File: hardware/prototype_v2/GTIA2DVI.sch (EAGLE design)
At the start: 25 parts, among them IC2 74AC541DW, IC4 GTIA, IC5 GTIA

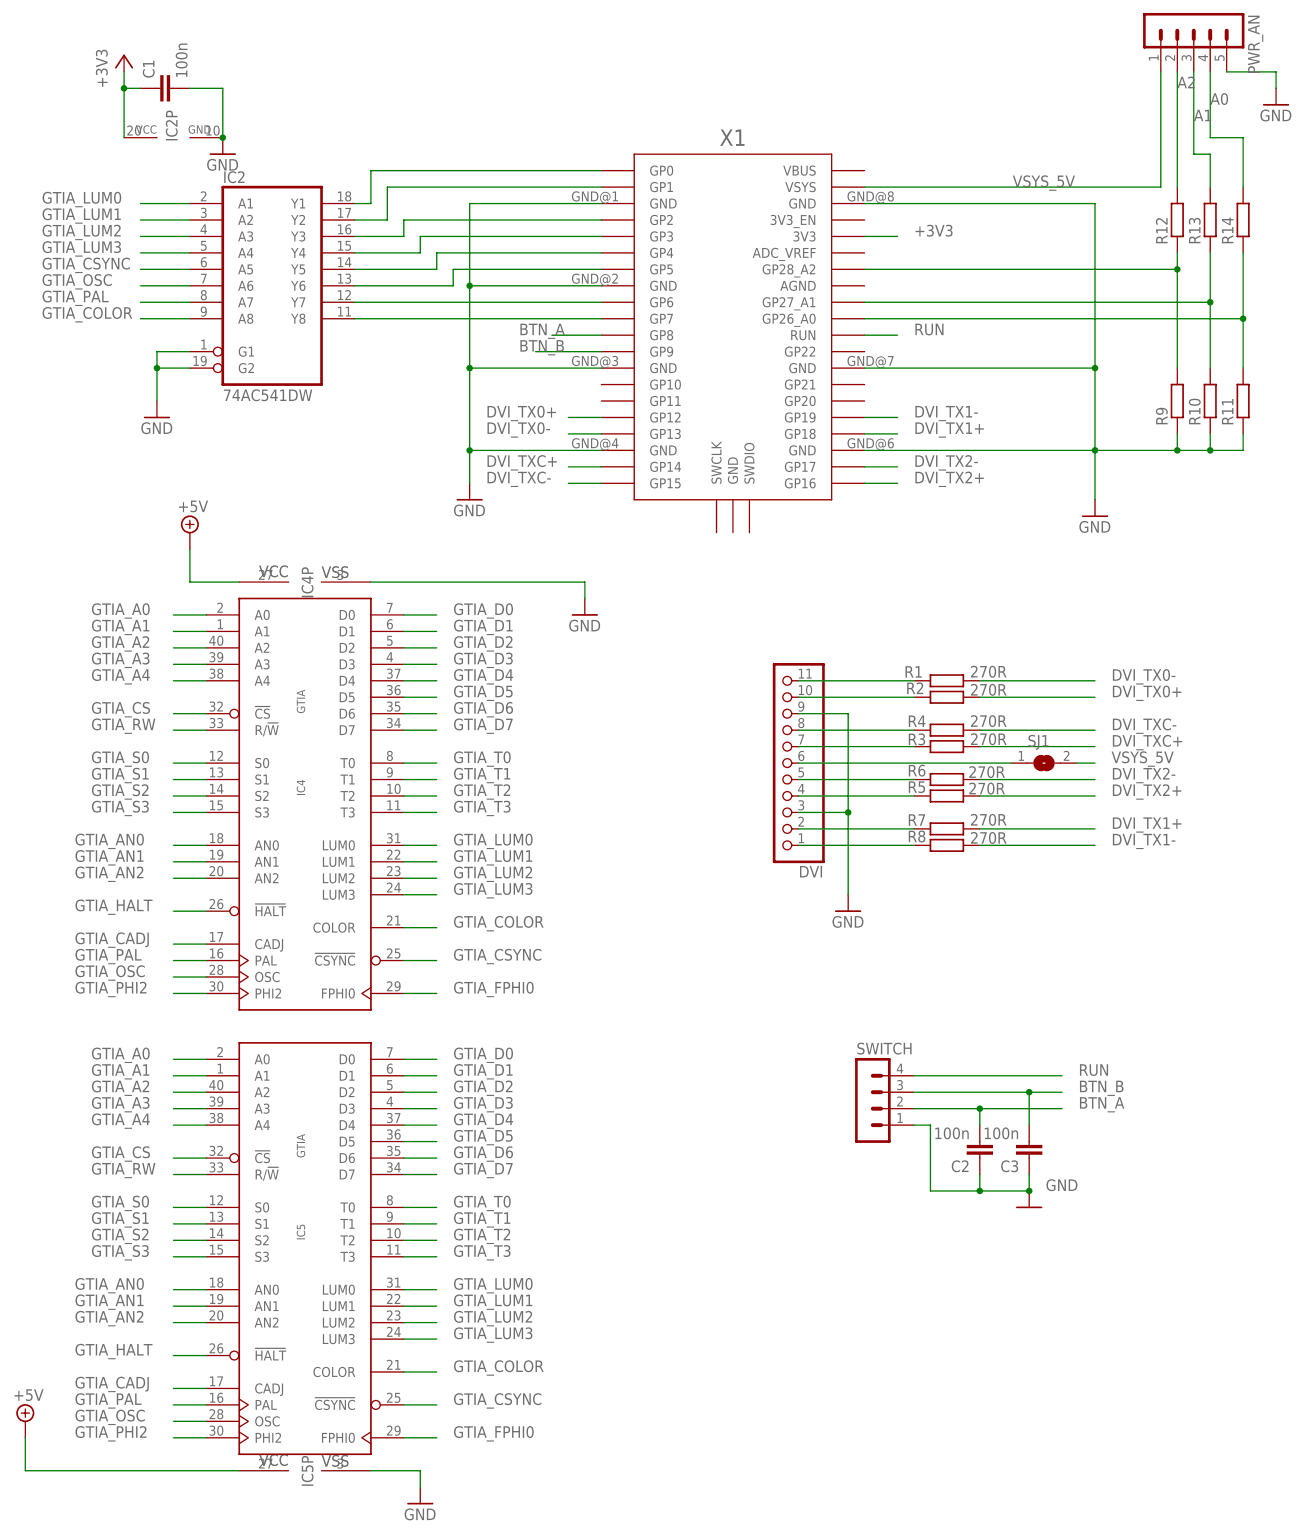
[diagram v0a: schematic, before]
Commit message: moved to hardware UART buttons and UART pins changed
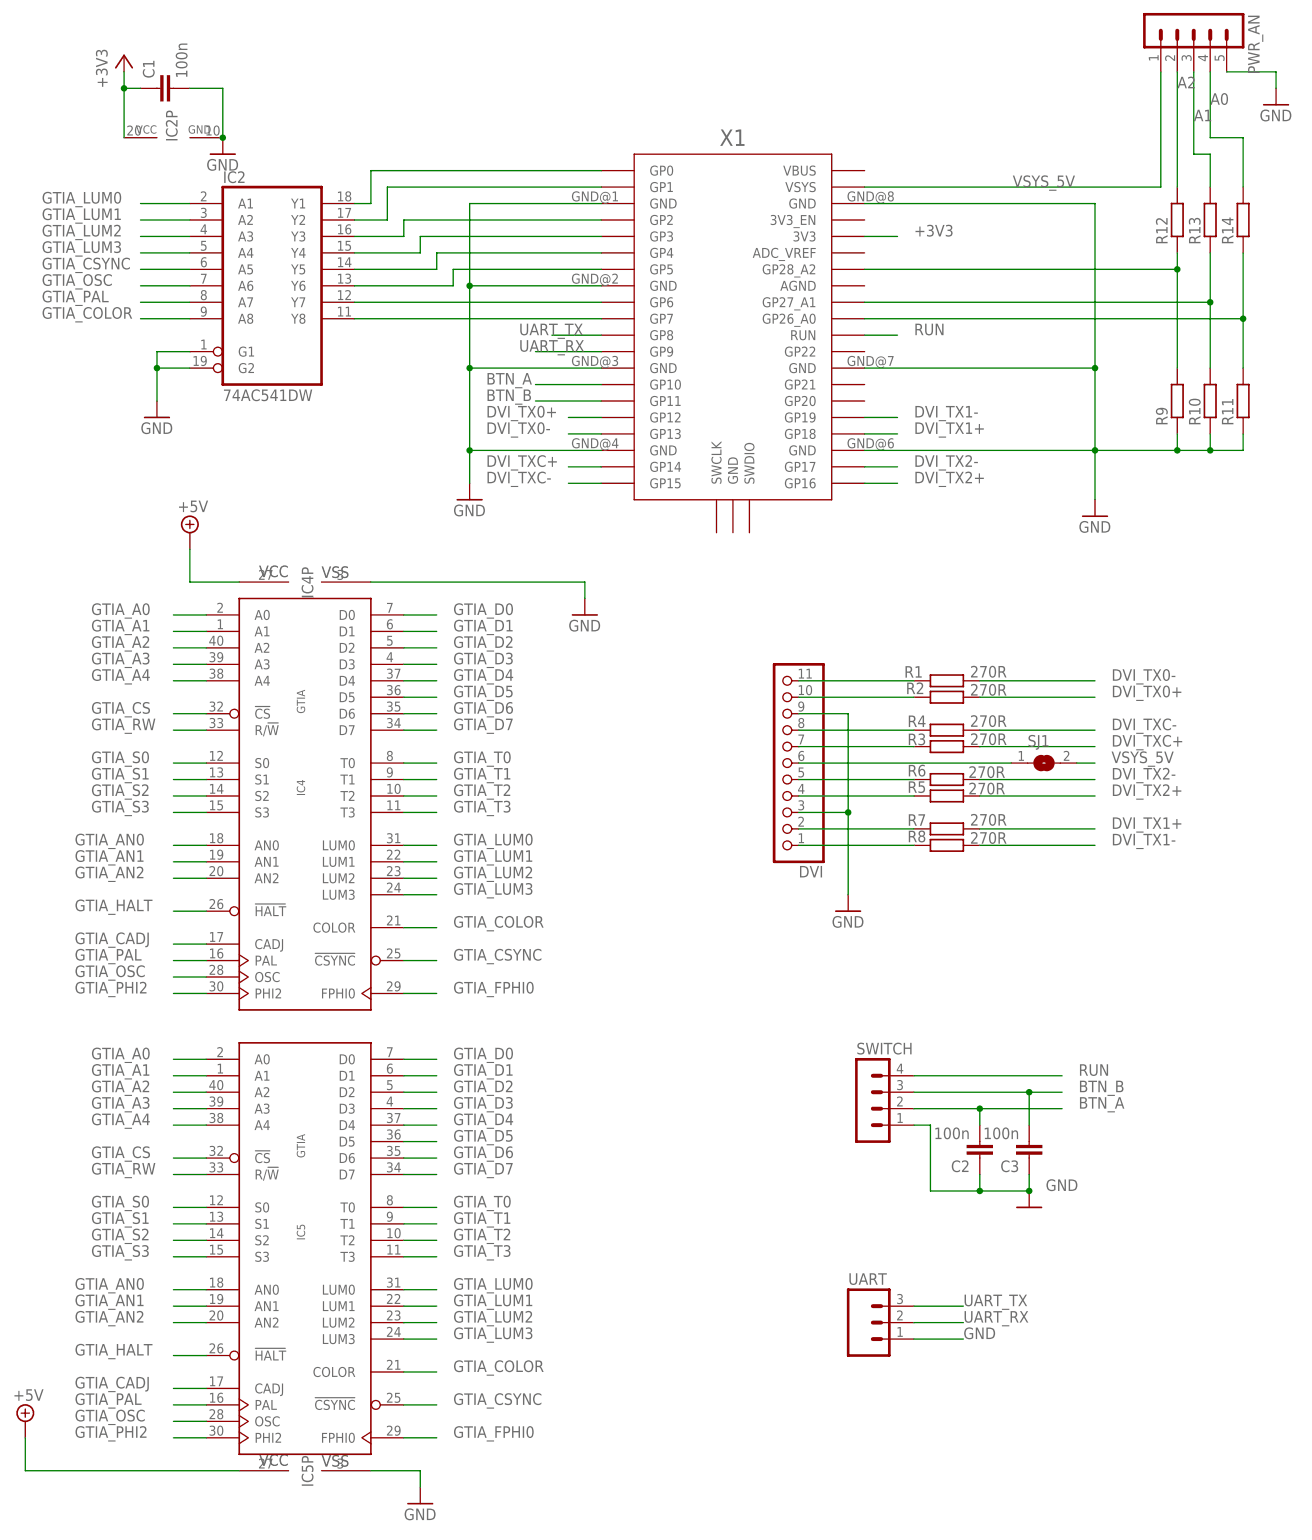
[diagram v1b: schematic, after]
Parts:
- added UART: (no value), con-amp-quick:MA03
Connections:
- new net UART_RX: UART.2, X1.GP9
- new net UART_TX: UART.3, X1.GP8
- net BTN_A: now also X1.GP10; no longer X1.GP8
- net BTN_B: now also X1.GP11; no longer X1.GP9
- net GND: now also UART.1
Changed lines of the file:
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@@
 <part name="C3" library="rcl" library_urn="urn:adsk.eagle:library:334" deviceset="C-EU" device="C0805" package3d_urn="urn:adsk.eagle:package:23617/2" value="100n"/>
 <part name="SJ1" library="jumper" library_urn="urn:adsk.eagle:library:252" deviceset="SJ" device="" package3d_urn="urn:adsk.eagle:package:15471/1"/>
+<part name="UART" library="con-amp-quick" library_urn="urn:adsk.eagle:library:125" deviceset="MA03" device="" package3d_urn="urn:adsk.eagle:package:5957/1"/>
 </parts>
 <sheets>
@@
 <attribute name="NAME" x="263.906" y="17.78" size="1.778" layer="95"/>
 <attribute name="VALUE" x="263.906" y="11.43" size="1.778" layer="96"/>
+</instance>
+<instance part="UART" gate="G$1" x="238.76" y="-71.12" smashed="yes">
+<attribute name="VALUE" x="236.22" y="-78.74" size="1.778" layer="96"/>
+<attribute name="NAME" x="236.22" y="-65.278" size="1.778" layer="95"/>
 </instance>
 </instances>
@@
 <junction x="256.54" y="-50.8"/>
 </segment>
+<segment>
+<pinref part="UART" gate="G$1" pin="1"/>
+<wire x1="246.38" y1="-73.66" x2="254" y2="-73.66" width="0.1524" layer="91"/>
+<label x="254" y="-73.66" size="1.778" layer="95"/>
+</segment>
 </net>
 <net name="+3V3" class="0">
@@
 </segment>
 <segment>
-<pinref part="X1" gate="G$1" pin="GP8"/>
-<wire x1="198.12" y1="81.28" x2="190.5" y2="81.28" width="0.1524" layer="91"/>
-<label x="185.42" y="81.28" size="1.778" layer="95"/>
+<pinref part="X1" gate="G$1" pin="GP10"/>
+<wire x1="198.12" y1="73.66" x2="187.96" y2="73.66" width="0.1524" layer="91"/>
+<label x="180.34" y="73.66" size="1.778" layer="95"/>
 </segment>
 </net>
@@
 </segment>
 <segment>
+<pinref part="X1" gate="G$1" pin="GP11"/>
+<wire x1="198.12" y1="71.12" x2="187.96" y2="71.12" width="0.1524" layer="91"/>
+<label x="180.34" y="71.12" size="1.778" layer="95"/>
+</segment>
+</net>
+<net name="RUN" class="0">
+<segment>
+<pinref part="SWITCH" gate="1" pin="4"/>
+<wire x1="246.38" y1="-33.02" x2="269.24" y2="-33.02" width="0.1524" layer="91"/>
+<label x="271.78" y="-33.02" size="1.778" layer="95"/>
+</segment>
+<segment>
+<pinref part="X1" gate="G$1" pin="RUN"/>
+<wire x1="238.76" y1="81.28" x2="243.84" y2="81.28" width="0.1524" layer="91"/>
+<label x="246.38" y="81.28" size="1.778" layer="95"/>
+</segment>
+</net>
+<net name="DVI_TX0+" class="0">
+<segment>
+<pinref part="R2" gate="G$1" pin="2"/>
+<wire x1="256.54" y1="25.4" x2="274.32" y2="25.4" width="0.1524" layer="91"/>
+<label x="276.86" y="25.4" size="1.778" layer="95"/>
+</segment>
+<segment>
+<pinref part="X1" gate="G$1" pin="GP12"/>
+<wire x1="193.04" y1="68.58" x2="198.12" y2="68.58" width="0.1524" layer="91"/>
+<label x="180.34" y="68.58" size="1.778" layer="95"/>
+</segment>
+</net>
+<net name="DVI_TX0-" class="0">
+<segment>
+<pinref part="R1" gate="G$1" pin="2"/>
+<wire x1="274.32" y1="27.94" x2="256.54" y2="27.94" width="0.1524" layer="91"/>
+<label x="276.86" y="27.94" size="1.778" layer="95"/>
+</segment>
+<segment>
+<pinref part="X1" gate="G$1" pin="GP13"/>
+<wire x1="198.12" y1="66.04" x2="193.04" y2="66.04" width="0.1524" layer="91"/>
+<label x="180.34" y="66.04" size="1.778" layer="95"/>
+</segment>
+</net>
+<net name="UART_TX" class="0">
+<segment>
+<pinref part="X1" gate="G$1" pin="GP8"/>
+<wire x1="198.12" y1="81.28" x2="190.5" y2="81.28" width="0.1524" layer="91"/>
+<label x="185.42" y="81.28" size="1.778" layer="95"/>
+</segment>
+<segment>
+<pinref part="UART" gate="G$1" pin="3"/>
+<wire x1="246.38" y1="-68.58" x2="254" y2="-68.58" width="0.1524" layer="91"/>
+<label x="254" y="-68.58" size="1.778" layer="95"/>
+</segment>
+</net>
+<net name="UART_RX" class="0">
+<segment>
 <pinref part="X1" gate="G$1" pin="GP9"/>
 <wire x1="198.12" y1="78.74" x2="187.96" y2="78.74" width="0.1524" layer="91"/>
 <label x="185.42" y="78.74" size="1.778" layer="95"/>
 </segment>
-</net>
-<net name="RUN" class="0">
-<segment>
-<pinref part="SWITCH" gate="1" pin="4"/>
-<wire x1="246.38" y1="-33.02" x2="269.24" y2="-33.02" width="0.1524" layer="91"/>
-<label x="271.78" y="-33.02" size="1.778" layer="95"/>
-</segment>
-<segment>
-<pinref part="X1" gate="G$1" pin="RUN"/>
-<wire x1="238.76" y1="81.28" x2="243.84" y2="81.28" width="0.1524" layer="91"/>
-<label x="246.38" y="81.28" size="1.778" layer="95"/>
-</segment>
-</net>
-<net name="DVI_TX0+" class="0">
-<segment>
-<pinref part="R2" gate="G$1" pin="2"/>
-<wire x1="256.54" y1="25.4" x2="274.32" y2="25.4" width="0.1524" layer="91"/>
-<label x="276.86" y="25.4" size="1.778" layer="95"/>
-</segment>
-<segment>
-<pinref part="X1" gate="G$1" pin="GP12"/>
-<wire x1="193.04" y1="68.58" x2="198.12" y2="68.58" width="0.1524" layer="91"/>
-<label x="180.34" y="68.58" size="1.778" layer="95"/>
-</segment>
-</net>
-<net name="DVI_TX0-" class="0">
-<segment>
-<pinref part="R1" gate="G$1" pin="2"/>
-<wire x1="274.32" y1="27.94" x2="256.54" y2="27.94" width="0.1524" layer="91"/>
-<label x="276.86" y="27.94" size="1.778" layer="95"/>
-</segment>
-<segment>
-<pinref part="X1" gate="G$1" pin="GP13"/>
-<wire x1="198.12" y1="66.04" x2="193.04" y2="66.04" width="0.1524" layer="91"/>
-<label x="180.34" y="66.04" size="1.778" layer="95"/>
-</segment>
-</net>
+<segment>
+<pinref part="UART" gate="G$1" pin="2"/>
+<wire x1="246.38" y1="-71.12" x2="254" y2="-71.12" width="0.1524" layer="91"/>
+<label x="254" y="-71.12" size="1.778" layer="95"/>
+</segment>
+</net>
